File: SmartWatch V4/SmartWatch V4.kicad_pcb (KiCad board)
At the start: 2 copper layers, 64 parts, among them J1 10118192-0001LF, J10 TestPad, J11 TestPad, J12 TestPad, J13 TestPad, J14 TestPad, J2 , J3 TestPad, J4 TestPad, J5 TestPad, J6 TestPad, J7 TestPad, J8 TestPad, J9 TestPad, Q1 FDN340P, Q2 MMBT3904, Q3 MMBT3904, Q4 FDN340P, SW1 EVQ-P7J01P, SW2 EVQ-P7J01P, U1 MAX17048, U10 TSC2003IPWR, U11 NHD-1.8-128160EF-CTXI#-T, U2 FT231XS, U3 LP5912-3.3DRVT, U4 LP5912-2.8DRVT, U5 MCP73832-2-OT, U6 ESP32-WROOM-32, U7 NLSV4T244, U8 NLSV4T244, U9 NLSV4T244

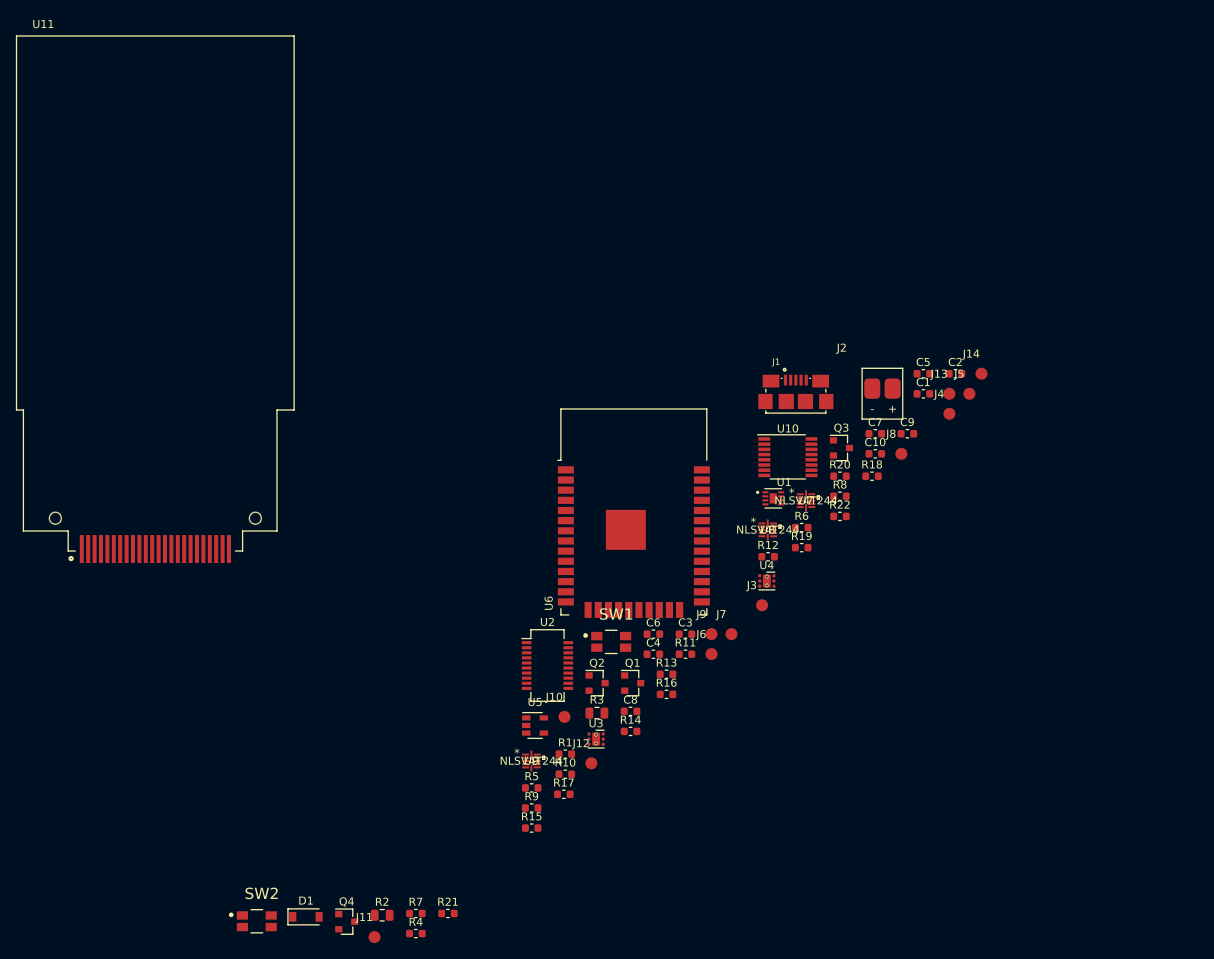
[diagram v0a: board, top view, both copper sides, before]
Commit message: Completed work of schematic and board layout of revision 4
Also began work on new body for the watch
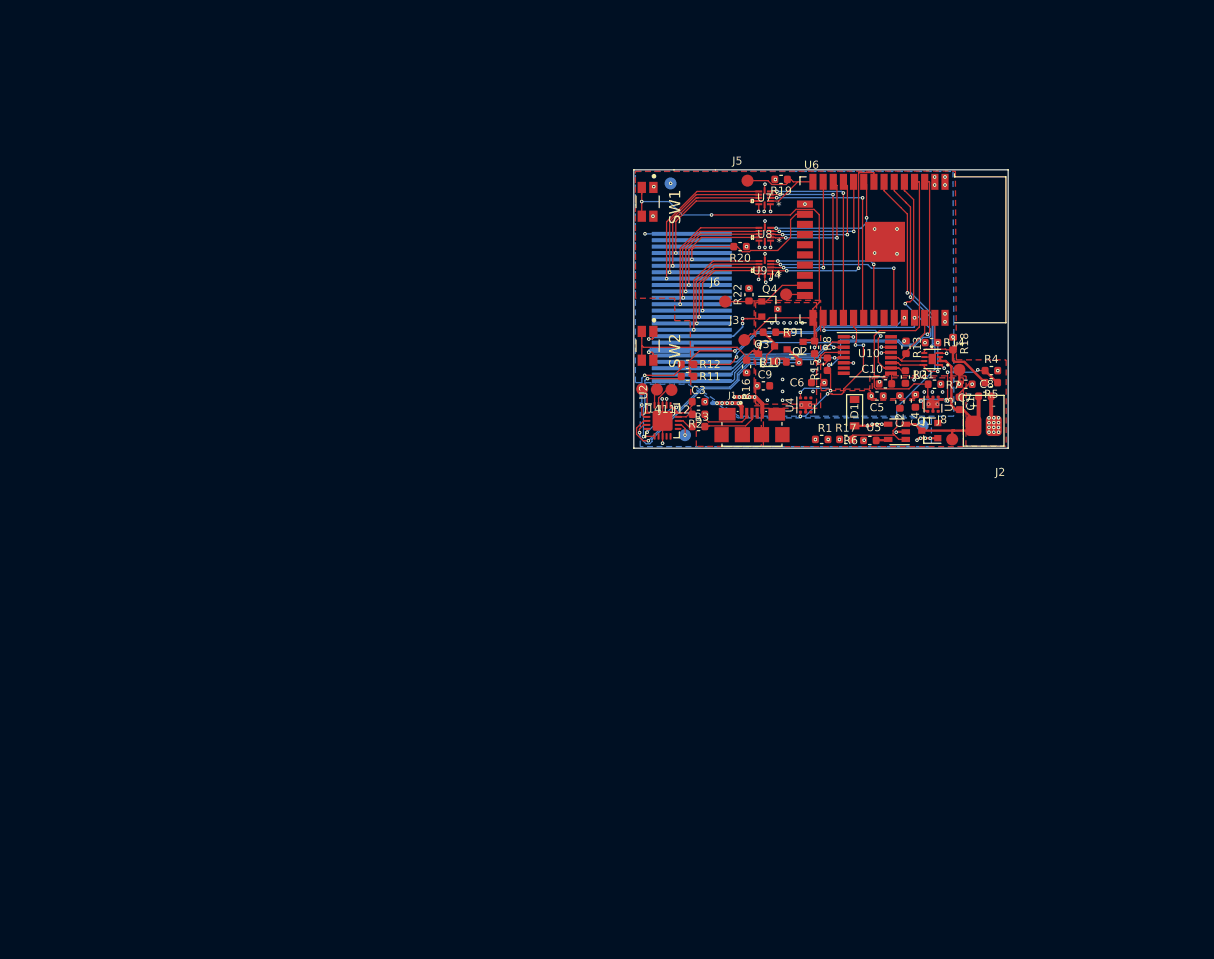
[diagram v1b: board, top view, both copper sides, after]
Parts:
- J10, J13, J7, U11: moved to B.Cu
- R2, R3: footprint Resistor_SMD:R_0805_2012Metric -> Resistor_SMD:R_0603_1608Metric
- U2: value FT231XS -> FT231XQ; footprint Package_SO:SSOP-20_3.9x8.7mm_P0.635mm -> Package_DFN_QFN:QFN-20-1EP_4x4mm_P0.5mm_EP2.5x2.5mm
- moved R4 100.6 mm to (167.9, 87.5)
- moved D1 93.1 mm to (150.8, 92.8), turned to 270 degrees
- moved Q4 93.1 mm to (140.2, 79.8)
- moved R7 92.6 mm to (160.8, 89.2), turned to 180 degrees
- moved R21 88.1 mm to (157.2, 88.3), turned to 90 degrees
- moved SW2 86.9 mm to (124.9, 84.4), turned to 270 degrees
- moved J11 77.0 mm to (126.1, 89.9), turned to 180 degrees
- moved R5 76.6 mm to (167.9, 89.0), turned to 180 degrees
- moved R2 74.1 mm to (131.3, 93.0), turned to 180 degrees
- moved U11 70.6 mm to (127.2, 79.6), turned to 270 degrees
- moved R15 69.7 mm to (145.8, 84.6), turned to 90 degrees
- moved U9 68.3 mm to (139.6, 74.6), turned to 180 degrees
- moved J10 68.0 mm to (127.8, 64.1)
- moved R9 66.5 mm to (140.2, 82.7), turned to 180 degrees
- moved R14 61.5 mm to (160.4, 84.0)
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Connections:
- net Net-(C2-Pad1) renamed /PWR_IN
- U2 pad 1: /DTR -> /RXD
- U2 pad 10: Net-(J13-Pad1) -> Net-(C3-Pad1)
- U2 pad 11: Net-(R3-Pad2) -> Net-(C3-Pad1)
- U2 pad 12: Net-(R2-Pad2) -> +3V3
- U2 pad 13: Net-(C3-Pad1) -> GND
- U2 pad 14: Net-(C3-Pad1) -> Net-(J12-Pad1)
- U2 pad 15: +3V3 -> Net-(J11-Pad1)
- U2 pad 16: GND -> Net-(J14-Pad1)
- U2 pad 17: Net-(J12-Pad1) -> /TXD
- U2 pad 18: Net-(J11-Pad1) -> /DTR
- U2 pad 19: Net-(J14-Pad1) -> /RTS
- U2 pad 2: /RTS -> Net-(U2-Pad2)
- U2 pad 20: /TXD -> Net-(C3-Pad1)
- U2 pad 3: Net-(C3-Pad1) -> GND
- U2 pad 4: /RXD -> Net-(U2-Pad4)
- U2 pad 6: GND -> Net-(U2-Pad6)
- U2 pad 7: Net-(U2-Pad7) -> Net-(J13-Pad1)
- U2 pad 8: Net-(U2-Pad8) -> Net-(R3-Pad2)
- U2 pad 9: Net-(U2-Pad9) -> Net-(R2-Pad2)
- U6 pad 10: /LCD_DB3 -> /LCD_DB2
- U6 pad 11: /LCD_DB4 -> /LCD_DB1
- U6 pad 12: /LCD_DB5 -> /LCD_DB0
- U6 pad 13: /LCD_~DC~ -> /LCD_DB5
- U6 pad 30: /LCD_DB0 -> /LCD_~DC~
- U6 pad 31: /LCD_DB1 -> /LCD_DB7
- U6 pad 33: /I2C_SDA -> /LCD_DB6
- U6 pad 37: /LCD_DB2 -> /I2C_SDA
- U6 pad 8: /LCD_DB6 -> /LCD_DB4
- U6 pad 9: /LCD_DB7 -> /LCD_DB3
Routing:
- net /EN: track 0.00 -> 62.2 mm, vias 0 -> 2
- net GND: track 0.00 -> 57.6 mm, vias 0 -> 57
- net /IO0: track 0.00 -> 54.9 mm, vias 0 -> 2
- net /LCD_PG: track 0.00 -> 45.7 mm, vias 0 -> 4
- net /CHG_STAT: track 0.00 -> 44.2 mm, vias 0 -> 2
- net /REG_PG: track 0.00 -> 39.9 mm
- net /BAT_ALRT: track 0.00 -> 33.4 mm, vias 0 -> 2
- net /TXD0: track 0.00 -> 31.6 mm, vias 0 -> 2
- net /RXD0: track 0.00 -> 31.0 mm, vias 0 -> 2
- net /DTR: track 0.00 -> 29.9 mm, vias 0 -> 2
- net /RTS: track 0.00 -> 28.4 mm, vias 0 -> 2
- net /LCD_~DC~: track 0.00 -> 26.6 mm, vias 0 -> 2
- net /LCD_DB4: track 0.00 -> 26.1 mm, vias 0 -> 2
- net /BAT+: track 0.00 -> 25.7 mm
- net /LCD_~RD~: track 0.00 -> 24.8 mm, vias 0 -> 2
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- added copper zone on F.Cu, net (none)
- added copper zone on B.Cu, net +2V8
- added copper zone on F.Cu, net +2V8
- added copper zone on F.Cu, net +3V3
- added copper zone on In1.Cu, net +3V3
- added copper zone on F.Cu, net /PWR_IN
- added copper zone on B.Cu, net /VBUS
- added copper zone on In2.Cu, net GND
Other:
- board outline added: 46.8 x 34.8 mm
- copper layers 2 -> 4
- net class Default: clearance 0.2 -> 0.1; trace_width 0.25 -> 0.1; via_dia 0.8 -> 0.45; via_drill 0.4 -> 0.2
- rule pad_to_mask_clearance: 0.051 -> 0
- rule trace_clearance: 0.2 -> 0.1
- rule trace_min: 0.2 -> 0.09
- rule via_min_drill: 0.3 -> 0.2
- rule via_min_size: 0.4 -> 0

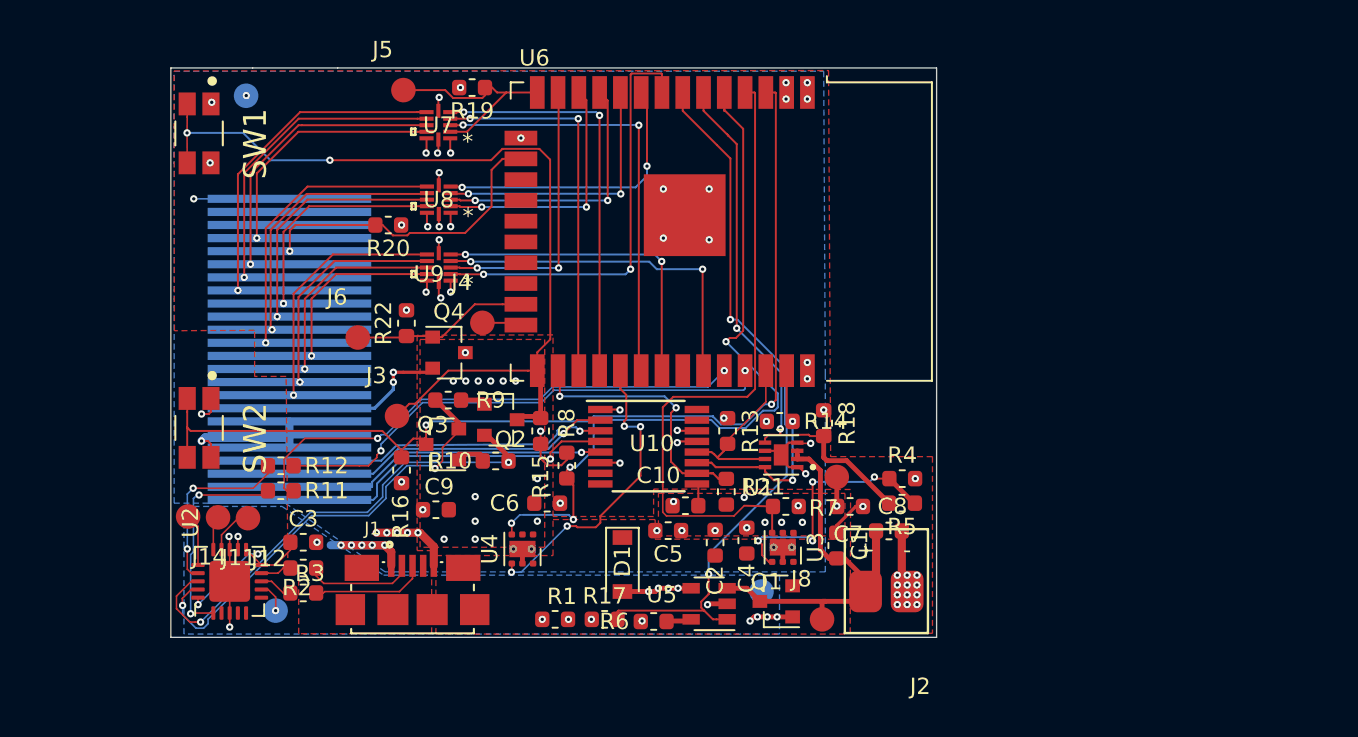
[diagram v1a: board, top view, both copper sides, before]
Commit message: Switched to MAX17260 due to availability
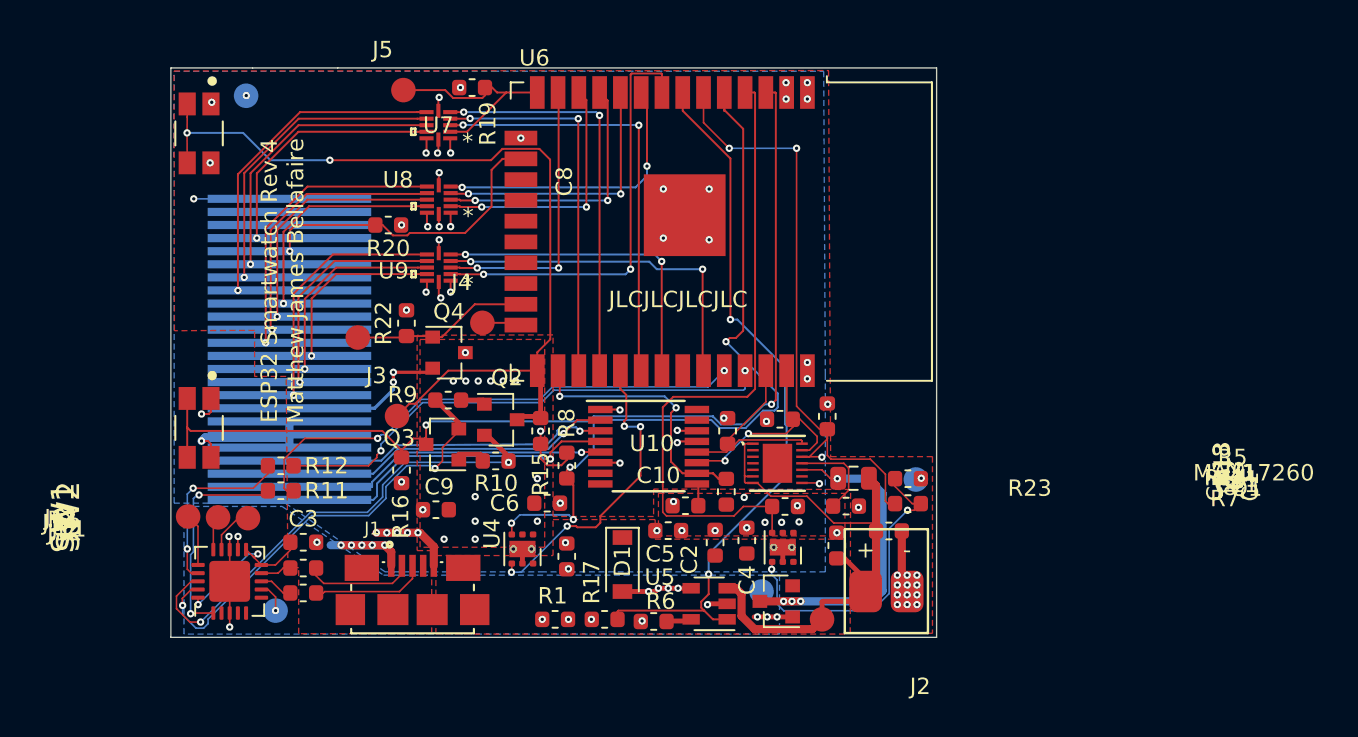
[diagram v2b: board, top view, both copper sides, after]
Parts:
- added C11: 0.1uF, Capacitor_SMD:C_0603_1608Metric, F.Cu at (164.5, 89.2)
- added R23: 6m, Resistor_SMD:R_0805_2012Metric, F.Cu at (164.9, 87.5)
- J9: moved to B.Cu
- U1: value MAX17048 -> MAX17260; footprint CustomFootprints:SON50P200X200X80-9N -> CustomFootprints:TDFN16-EP
- moved C8 17.6 mm to (147.4, 92.3), turned to 90 degrees
- moved J9 4.83 mm to (168.7, 87.6), turned to 270 degrees
- moved U1 0.56 mm to (160.3, 86.6), turned to 0 degrees
- moved R18 0.47 mm to (163.3, 83.7)
- moved R5 0.36 mm to (168.2, 89.0)
- moved R4 0.35 mm to (168.2, 87.5)
- moved R14 0.13 mm to (160.4, 83.9)
- moved R7 0.05 mm to (160.7, 89.2)
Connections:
- Q1 pad 3: /BAT+ -> /BAT_SENSE
- U1 pad 1: GND -> /BAT+
- U1 pad 2: /BAT+ -> (no net)
- U1 pad 3: /BAT+ -> (no net)
- U1 pad 4: GND -> (no net)
- U1 pad 5: /BAT_ALRT -> (no net)
- U1 pad 6: GND -> /BAT+
- U1 pad 7: /I2C_SCL -> /BAT+
- U1 pad 8: /I2C_SDA -> GND
- U1 pad 9: GND -> Net-(U1-Pad9)
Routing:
- net /BAT_SENSE: track 0.00 -> 20.3 mm, vias 0 -> 4
- net /BAT+: track 25.7 -> 35.3 mm
- net GND: track 57.6 -> 50.9 mm, vias 57 -> 58
- net Net-(C11-Pad1): track 0.00 -> 5.70 mm
- net /BAT_ALRT: track 33.4 -> 37.8 mm, vias 2 -> 3
- net /LDO_EN: track 15.9 -> 19.2 mm, vias 4 -> 2
- net /I2C_SCL: track 11.3 -> 13.2 mm
- net +3V3: track 10.4 -> 8.78 mm
- net /VBUS: track 17.1 -> 16.7 mm, vias 14 -> 13
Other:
- rule solder_mask_min_width: 0.25 -> 0.01
- board text added: "ESP32 Smartwatch Rev 4 Matthew James Bellafaire"
- board text added: "JLCJLCJLCJLC"

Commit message: Changes to version 4 before sending off to production
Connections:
- J1 pad SH1: (no net) -> GND
- J1 pad SH2: (no net) -> GND
- J1 pad SH3: (no net) -> GND
- J1 pad SH4: (no net) -> GND
- J1 pad SH5: (no net) -> GND
- J1 pad SH6: (no net) -> GND
- Q4 pad 1: /IO15 -> /LCD_LED
- R22 pad 2: /IO15 -> /LCD_LED
- U1 pad 15: (no net) -> GND
- U1 pad 9: Net-(U1-Pad9) -> GND
- U4 pad 4: /LCD_EN -> /IO12
- U6 pad 27: /LCD_~WR~ -> /LCD_LED
- U6 pad 29: /LCD_EN -> /LCD_~CS~
- U6 pad 34: /TXD0 -> /RXD0
- U6 pad 35: /RXD0 -> /TXD0
- U7 pad 2: /IO12 -> /LCD_~CS~
- U7 pad 4: /LCD_~WR~ -> /IO15
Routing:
- net /IO12: track 13.5 -> 47.3 mm, vias 0 -> 4
- net /LCD_~CS~: track 0.00 -> 24.7 mm, vias 0 -> 2
- net /LCD_~WR~: track 23.2 -> 0.00 mm, vias 2 -> 0
- net /IO15: track 10.9 -> 32.8 mm, vias 0 -> 2
- net /LCD_EN: track 18.8 -> 0.00 mm, vias 4 -> 0
- net /LCD_LED: track 0.00 -> 12.2 mm, vias 0 -> 2
- net GND: track 50.9 -> 54.7 mm, vias 58 -> 66
- net /RXD0: track 31.0 -> 28.7 mm
- net /IO0: track 54.9 -> 57.1 mm
